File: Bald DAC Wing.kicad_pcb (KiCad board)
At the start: 4 copper layers, 52 x 46.5 mm, 50 parts, among them J1 PWR, J2 DAC_A_Out, J3 DAC_B_Out, J4 Data Debug HDR, J5 Z_Out, U1 AD5447, U2 AD8065ARTZ, U3 AD8065ARTZ, U4 74LVC574APWR, U5 74LVC574APWR, U6 74LVC1G04, U7 REF3425

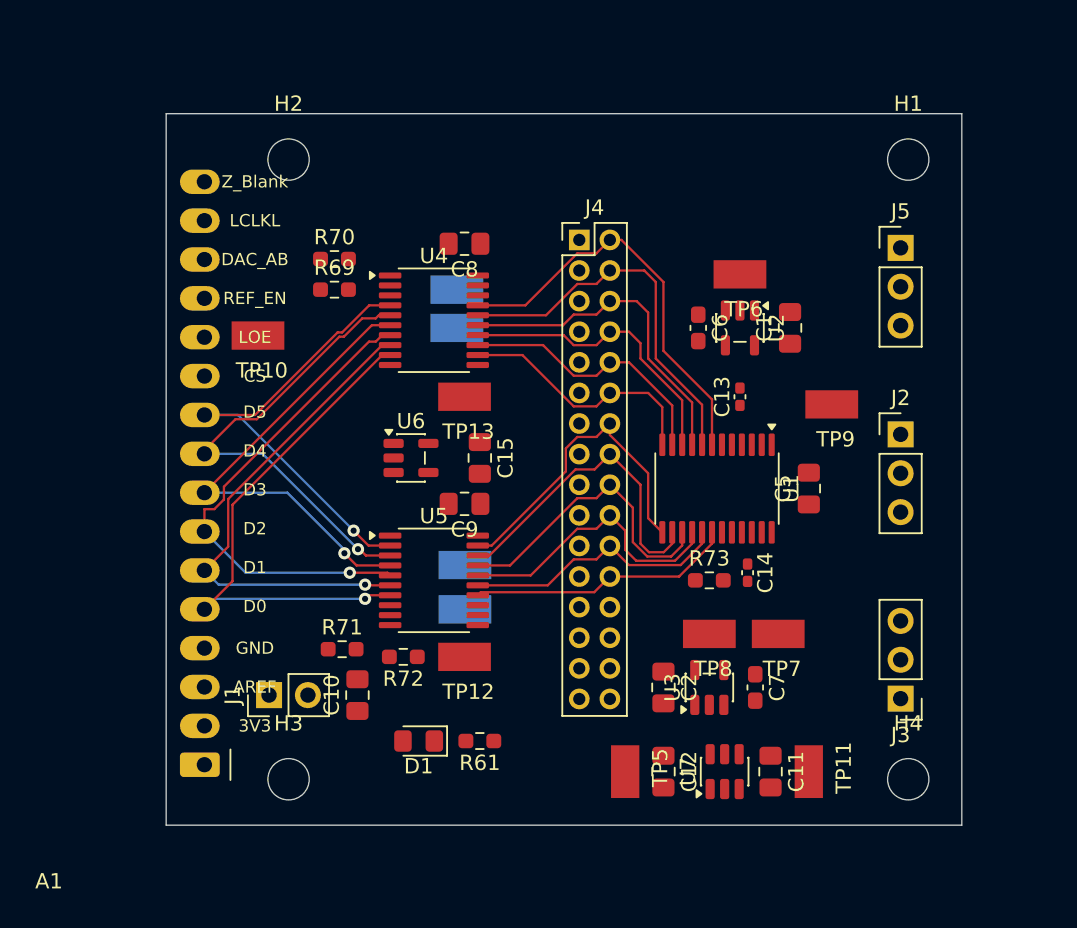
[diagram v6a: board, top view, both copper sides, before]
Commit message: ditched feather footprint and went discete. also realized board could be covering
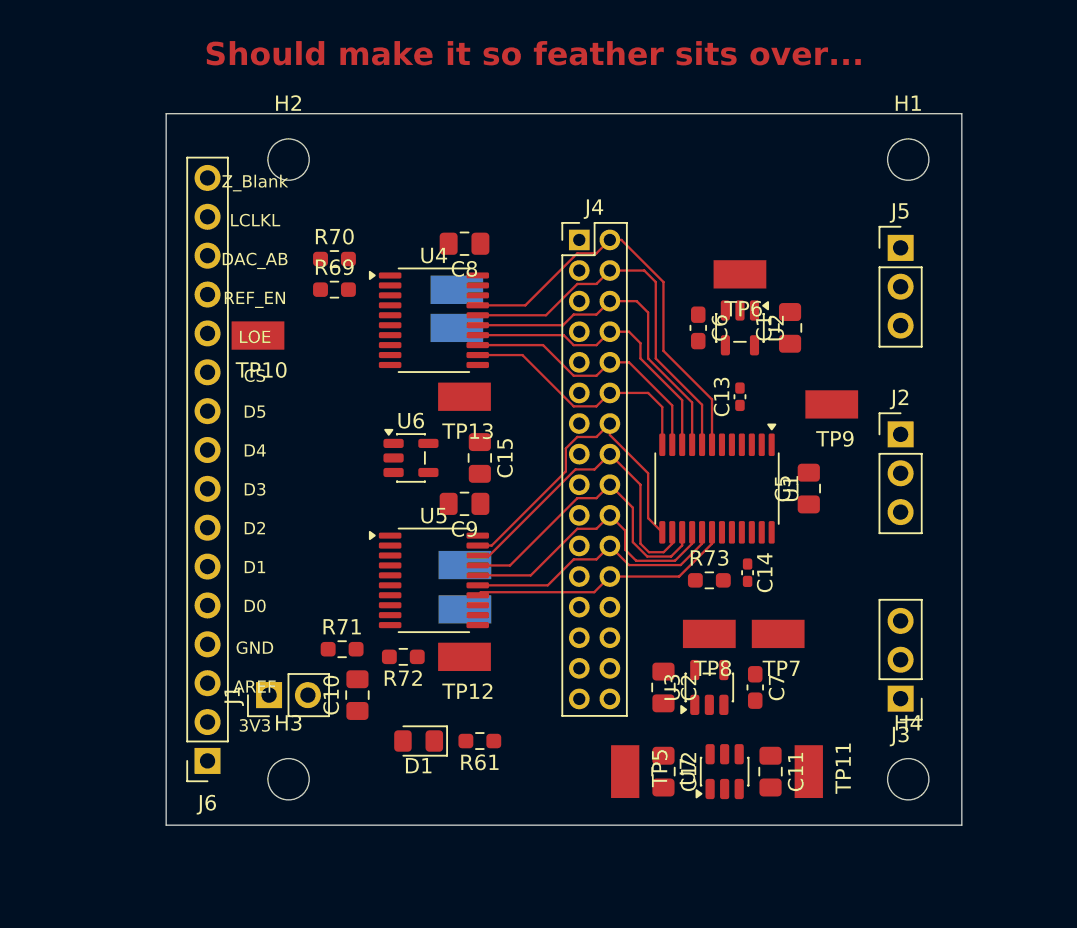
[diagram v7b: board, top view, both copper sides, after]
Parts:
- removed A1: Adafruit_Feather_Generic, Module:Adafruit_Feather
- added J6: Feather, Connector_PinSocket_2.54mm:PinSocket_1x16_P2.54mm_Vertical, F.Cu at (91.2, 110.3)
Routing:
- net /D0: track 34.5 -> 0.00 mm, vias 1 -> 0
- net /D1: track 32.6 -> 0.00 mm, vias 1 -> 0
- net /D2: track 32.1 -> 0.00 mm, vias 1 -> 0
- net /D4: track 30.9 -> 0.00 mm, vias 1 -> 0
- net /D3: track 30.9 -> 0.00 mm, vias 1 -> 0
- net /D5: track 30.8 -> 0.00 mm, vias 1 -> 0
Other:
- board text added: "Should make it so feather sits over..."

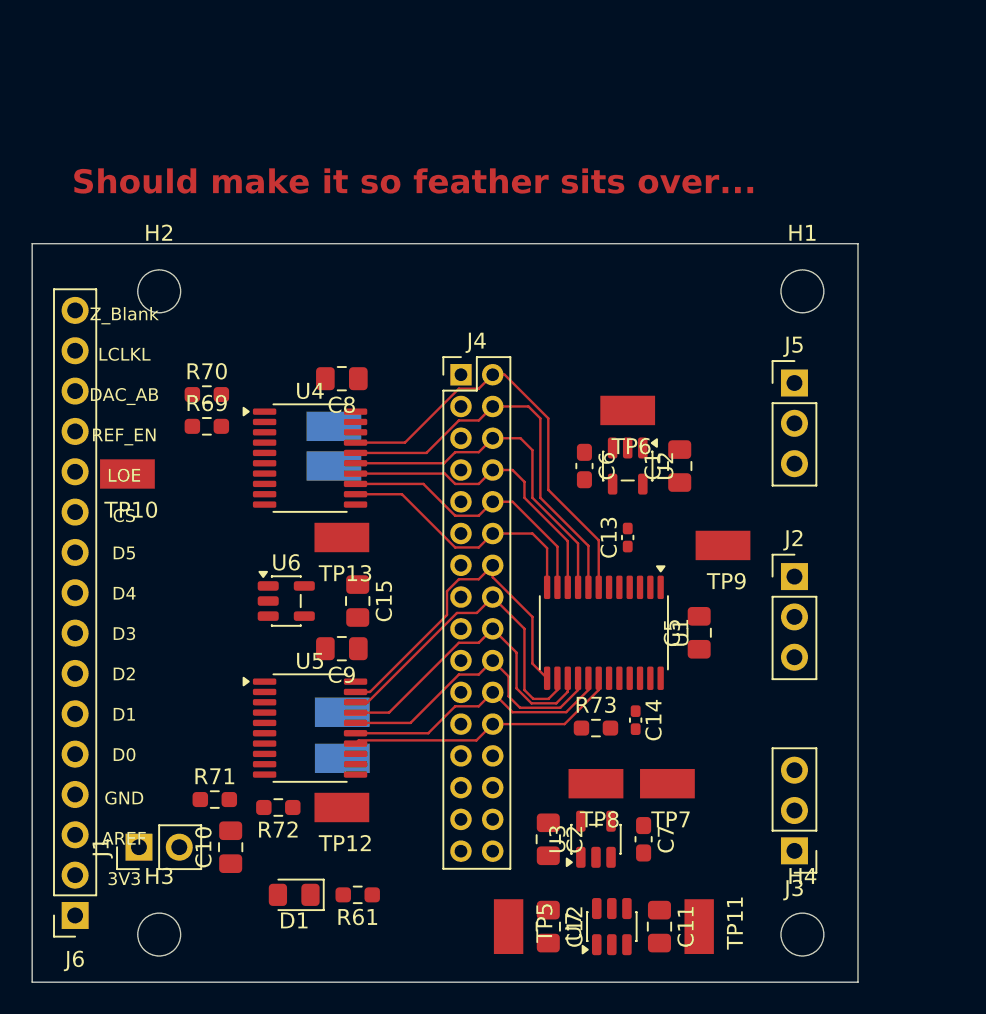
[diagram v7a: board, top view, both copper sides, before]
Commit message: broke-up debug headers and squeeshed the board some moar.
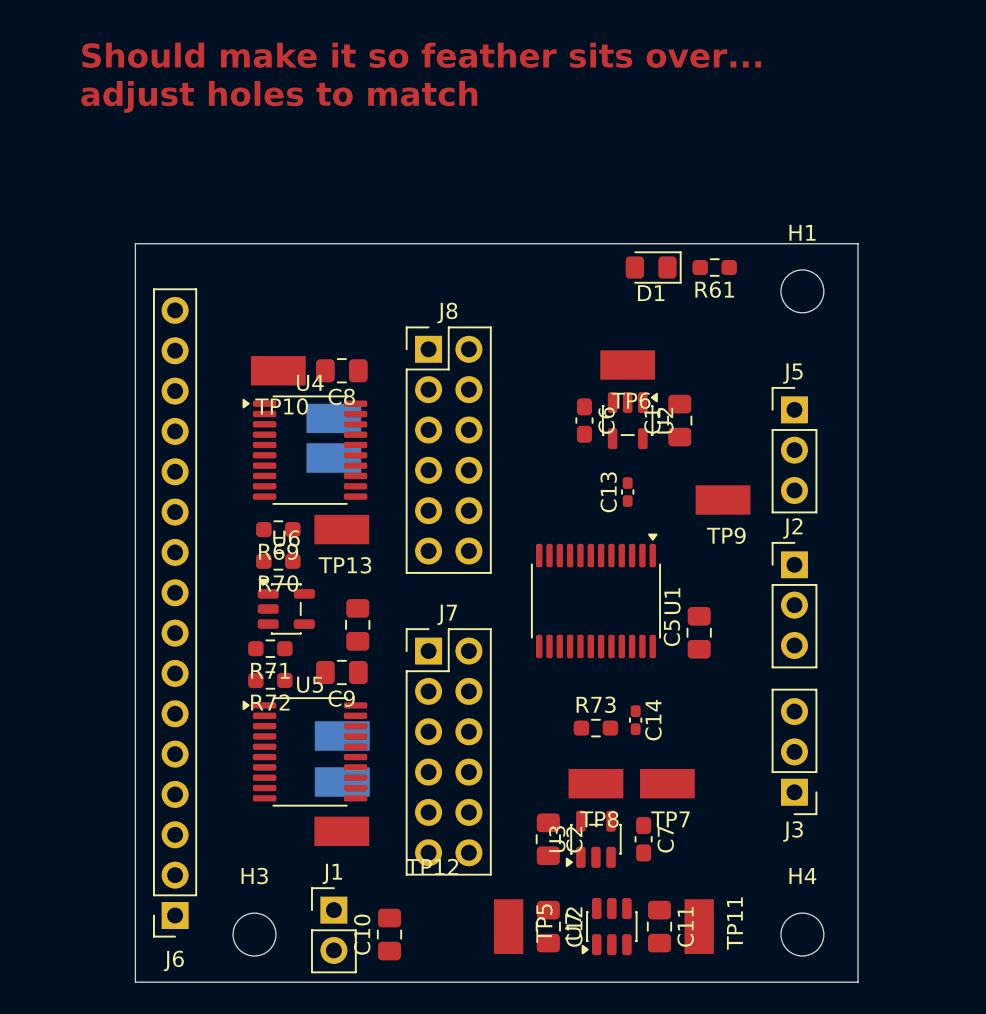
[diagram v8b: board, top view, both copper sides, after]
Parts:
- removed H2: MountingHole_M2.5_Screw, MountingHole:MountingHole_2.7mm_M2.5
- removed J4: Data Debug HDR, Connector_PinHeader_2.00mm:PinHeader_2x16_P2.00mm_Vertical
- added J7: Data Debug Low, Connector_PinHeader_2.54mm:PinHeader_2x06_P2.54mm_Vertical, F.Cu at (113.5, 93.7)
- added J8: High, Connector_PinHeader_2.54mm:PinHeader_2x06_P2.54mm_Vertical, F.Cu at (113.5, 74.7)
- moved D1 45.4 mm to (127.5, 69.5)
- moved R61 45.4 mm to (131.5, 69.5)
- moved J1 12.9 mm to (107.5, 110.0), turned to 0 degrees
- moved TP10 11.5 mm to (104.0, 76.0)
- moved R70 11.4 mm to (104.0, 88.0), turned to 180 degrees
- moved C10 11.4 mm to (111.0, 111.5)
- moved R71 10.1 mm to (103.5, 93.5), turned to 180 degrees
- moved R72 8.02 mm to (103.5, 95.5)
- moved R69 7.91 mm to (104.0, 86.0), turned to 180 degrees
- moved J6 6.30 mm to (97.5, 110.3)
- moved H3 6.00 mm to (102.5, 111.5)
- moved J3 3.69 mm to (136.5, 102.5)
- moved C1 2.86 mm to (129.3, 79.1)
- moved C13 2.86 mm to (126.0, 83.6)
- moved C6 2.86 mm to (123.3, 79.1)
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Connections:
- J6 pad 11: /~{CS} -> /LOE
- J6 pad 12: /LOE -> /~{CS}
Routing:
- net /DB11: track 27.0 -> 0.00 mm
- net /DB10: track 25.1 -> 0.00 mm
- net /DB9: track 21.9 -> 0.00 mm
- net /DB5: track 21.4 -> 0.00 mm
- net /DB4: track 21.3 -> 0.00 mm
- net /DB3: track 20.0 -> 0.00 mm
- net /DB8: track 19.3 -> 0.00 mm
- net /DB2: track 18.8 -> 0.00 mm
- net /DB7: track 17.6 -> 0.00 mm
- net /DB1: track 17.6 -> 0.00 mm
- net /DB0: track 17.4 -> 0.00 mm
- net /DB6: track 16.7 -> 0.00 mm
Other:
- board size 52 x 46.5 mm -> 45.5 x 46.5 mm
- board text added: "Should make it so feather sits over... adjust holes to match"
- board text removed: "3V3"
- board text removed: "AREF"
- board text removed: "CS"
- board text removed: "D0"
- board text removed: "D1"
- board text removed: "D2"
- board text removed: "D3"
- board text removed: "D4"
- board text removed: "D5"
- board text removed: "DAC_AB"
- board text removed: "GND"
- board text removed: "LCLKL"
- board text removed: "LOE"
- board text removed: "REF_EN"
- board text removed: "Should make it so feather sits over..."
- board text removed: "Z_Blank"
